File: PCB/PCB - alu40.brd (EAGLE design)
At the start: 228 x 76 mm, 163 parts, among them IC1 XB3303ASOT23, IC2 TP4054-42-SOT25-R, J1 SK-3296S-01-L1, J2 USB4510-03-1-A, Q2 PMOSFET, Q3 PMOSFET, Q5 PMOSFET, Q6 NMOSFET, U1 ISP1807-LRISP1807-LR_ISP1807-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, X1 BM02B-SRSS-TB

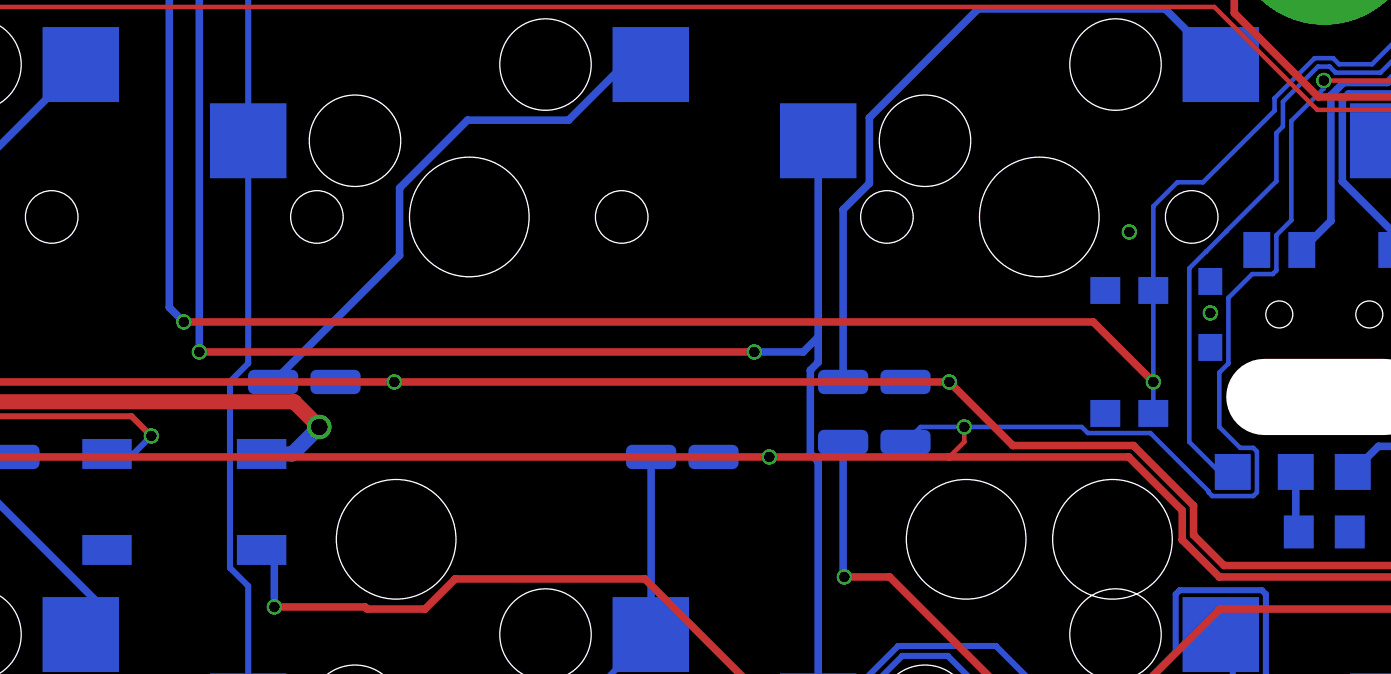
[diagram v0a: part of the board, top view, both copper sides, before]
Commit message: Move reset switch
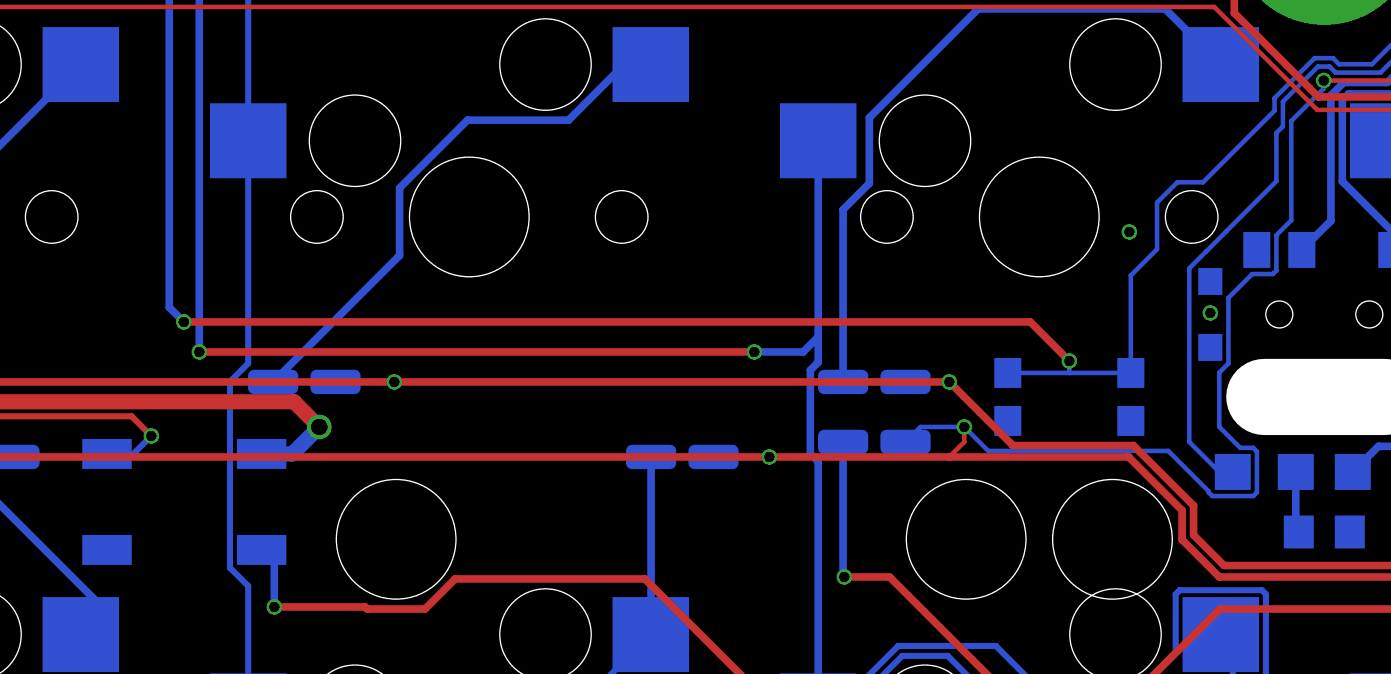
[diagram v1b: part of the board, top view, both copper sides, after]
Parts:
- moved S5 2.50 mm to (105.5, 22.5), turned to 0 degrees
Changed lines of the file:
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@@
 <attribute name="NAME" x="151.3" y="58.7" size="1.27" layer="26" rot="MR180" align="center"/>
 </element>
-<element name="S5" library="Volume_V1" library_urn="urn:adsk.eagle:library:32198814" package="TACTILE_SWITCH_SMD_4.6X2.8MM" package3d_urn="urn:adsk.eagle:package:32213842/2" value="MOMENTARY-SWITCH-SPST-SMD-4.6X2.8MM" x="107.5" y="24" smashed="yes" rot="MR90">
-<attribute name="NAME" x="109.405" y="24" size="0.6096" layer="26" font="vector" ratio="20" rot="MR90" align="bottom-center"/>
-<attribute name="PROD_ID" value="SWCH-13065" x="-31.5396" y="-53.5462" size="1.778" layer="28" rot="MR90" display="off"/>
-<attribute name="VALUE" x="105.595" y="24" size="0.6096" layer="28" font="vector" ratio="20" rot="MR90" align="top-center"/>
+<element name="S5" library="Volume_V1" library_urn="urn:adsk.eagle:library:32198814" package="TACTILE_SWITCH_SMD_4.6X2.8MM" package3d_urn="urn:adsk.eagle:package:32213842/2" value="MOMENTARY-SWITCH-SPST-SMD-4.6X2.8MM" x="105.5" y="22.5" smashed="yes" rot="MR0">
+<attribute name="NAME" x="105.5" y="24.405" size="0.6096" layer="26" font="vector" ratio="20" rot="MR0" align="bottom-center"/>
+<attribute name="PROD_ID" value="SWCH-13065" x="183.0462" y="-116.5396" size="1.778" layer="28" rot="MR0" display="off"/>
+<attribute name="VALUE" x="105.5" y="20.595" size="0.6096" layer="28" font="vector" ratio="20" rot="MR0" align="top-center"/>
 </element>
 <element name="Q5" library="Transistor" library_urn="urn:adsk.eagle:library:16378713" package="SOT23" package3d_urn="urn:adsk.eagle:package:28738/2" value="PMOSFET" x="151.5" y="41" smashed="yes" rot="MR90">
@@
 <wire x1="96.775" y1="42.35" x2="96.9471" y2="42.5221" width="0.1524" layer="16"/>
 <via x="96.9471" y="42.5221" extent="1-16" drill="0.35"/>
-<wire x1="108.3" y1="21.95" x2="108.3" y2="23" width="0.1524" layer="16"/>
-<wire x1="108.3" y1="23" x2="108.3" y2="26.05" width="0.1524" layer="16"/>
 <wire x1="81.96" y1="74.5" x2="81.96" y2="72.04" width="0.1524" layer="16"/>
 <wire x1="85.2267" y1="68.7733" x2="86.4416375" y2="68.7733" width="0.1524" layer="16"/>
@@
 <wire x1="107.4779" y1="42.5221" x2="96.9471" y2="42.5221" width="0.1524" layer="1"/>
 <wire x1="109.1012875" y1="29.6557" x2="109.9557" y2="29.6557" width="0.1524" layer="16"/>
-<wire x1="108.3" y1="26.05" x2="108.3" y2="28.8544125" width="0.1524" layer="16"/>
-<wire x1="108.3" y1="28.8544125" x2="109.1012875" y2="29.6557" width="0.1524" layer="16"/>
 <wire x1="87.65" y1="63" x2="87.65" y2="61.85" width="0.254" layer="16"/>
 <wire x1="87.65" y1="61.85" x2="88.5" y2="61" width="0.254" layer="16"/>
@@
 <wire x1="75.5" y1="25.4835" x2="75.9835" y2="25" width="0.254" layer="16"/>
 <via x="75.9835" y="25" extent="1-16" drill="0.35"/>
-<wire x1="75.9835" y1="25" x2="106.3" y2="25" width="0.254" layer="1"/>
-<wire x1="106.3" y1="25" x2="108.3" y2="23" width="0.254" layer="1"/>
-<via x="108.3" y="23" extent="1-16" drill="0.35"/>
+<wire x1="75.9835" y1="25" x2="104.2" y2="25" width="0.254" layer="1"/>
+<wire x1="104.2" y1="25" x2="105.5" y2="23.7" width="0.254" layer="1"/>
+<via x="105.5" y="23.7" extent="1-16" drill="0.35"/>
 <wire x1="112.3412" y1="32.0412" x2="112.3412" y2="32.4584125" width="0.1524" layer="16"/>
 <wire x1="112.3412" y1="32.4584125" x2="113.67485" y2="33.7920625" width="0.1524" layer="16"/>
@@
 <wire x1="114.4935875" y1="33.5906" x2="115.5906" y2="33.5906" width="0.1524" layer="16"/>
 <wire x1="109.445" y1="40.555" x2="107.4779" y2="42.5221" width="0.1524" layer="1"/>
+<wire x1="103.45" y1="23.3" x2="105.5" y2="23.3" width="0.1524" layer="16"/>
+<wire x1="105.5" y1="23.3" x2="107.55" y2="23.3" width="0.1524" layer="16"/>
+<wire x1="107.55" y1="23.3" x2="107.55" y2="26.55" width="0.1524" layer="16"/>
+<wire x1="108.4243" y1="28.9787125" x2="109.1012875" y2="29.6557" width="0.1524" layer="16"/>
+<wire x1="108.4243" y1="27.4243" x2="108.4243" y2="28.9787125" width="0.1524" layer="16"/>
+<wire x1="107.55" y1="26.55" x2="108.4243" y2="27.4243" width="0.1524" layer="16"/>
+<wire x1="105.5" y1="23.7" x2="105.5" y2="23.3" width="0.1524" layer="16"/>
 </signal>
 <signal name="POWER_PIN">
@@
 <wire x1="110.1468" y1="19.31583125" x2="110.1468" y2="19.3532" width="0.1524" layer="16"/>
 <via x="102" y="21.5" extent="1-16" drill="0.35"/>
-<wire x1="105.91263125" y1="21.5" x2="102" y2="21.5" width="0.1524" layer="16"/>
-<wire x1="106.11583125" y1="21.2968" x2="105.91263125" y2="21.5" width="0.1524" layer="16"/>
-<wire x1="108.2032" y1="21.2968" x2="106.11583125" y2="21.2968" width="0.1524" layer="16"/>
+<wire x1="108.8" y1="20.7" x2="102.8" y2="20.7" width="0.1524" layer="16"/>
+<wire x1="102" y1="21.5" x2="102.8" y2="20.7" width="0.1524" layer="16"/>
 <wire x1="102" y1="21.5" x2="102" y2="21" width="0.1524" layer="1"/>
 <wire x1="102" y1="21" x2="101.5" y2="20.5" width="0.1524" layer="1"/>
 <wire x1="110.5" y1="23.31263125" x2="110.5" y2="21.5" width="0.1524" layer="16"/>
 <wire x1="110.5" y1="21.5" x2="111.1968" y2="20.8032" width="0.1524" layer="16"/>
-<wire x1="110.1468" y1="19.3532" x2="108.2032" y2="21.2968" width="0.1524" layer="16"/>
+<wire x1="108.8" y1="20.7" x2="110.1468" y2="19.3532" width="0.1524" layer="16"/>
 <wire x1="100.04" y1="21" x2="100.54" y2="21.5" width="0.1524" layer="16"/>
 <wire x1="100.54" y1="21.5" x2="102" y2="21.5" width="0.1524" layer="16"/>

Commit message: Remove unnecessary swd pin
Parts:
- PROG1: device SparkFun-Connectors:1X06_1.27MM -> SparkFun-Connectors:1X05_1.27MM
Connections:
- net V_USB: no longer PROG1.6
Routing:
- net V_USB: track 243.9 -> 209.8 mm
- net ROW0: track 239.6 -> 240.4 mm
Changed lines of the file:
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@@
 <attribute name="VALUE" x="159.965" y="40.305" size="1.27" layer="28" rot="MR180"/>
 </element>
-<element name="PROG1" library="SparkFun-Connectors" library_urn="urn:adsk.eagle:library:513" package="1X06_1.27MM" package3d_urn="urn:adsk.eagle:package:38131/1" value="" x="84.5" y="74.5" smashed="yes" rot="MR0">
+<element name="PROG1" library="SparkFun-Connectors" library_urn="urn:adsk.eagle:library:513" package="1X05_1.27MM" package3d_urn="urn:adsk.eagle:package:38110/1" value="" x="84.5" y="74.5" smashed="yes" rot="MR0">
 <attribute name="NAME" x="84.881" y="75.516" size="0.6096" layer="26" font="vector" ratio="20" rot="MR0"/>
 <attribute name="VALUE" x="84.881" y="72.849" size="0.6096" layer="28" font="vector" ratio="20" rot="MR0"/>
@@
 <contactref element="IC2" pad="4"/>
 <contactref element="LED2" pad="A"/>
-<contactref element="PROG1" pad="6"/>
 <contactref element="D67" pad="A"/>
 <contactref element="D63" pad="2"/>
@@
 <wire x1="92.6793625" y1="45.5745" x2="93.5" y2="46.3951375" width="0.1524" layer="1"/>
 <wire x1="93.5" y1="46.3951375" x2="93.5" y2="48" width="0.1524" layer="1"/>
-<wire x1="78.15" y1="74.5" x2="79.15" y2="73.5" width="0.254" layer="1"/>
-<wire x1="102.5" y1="73.5" x2="106" y2="70" width="0.254" layer="1"/>
 <via x="126.5" y="70.5" extent="1-16" drill="0.35"/>
 <wire x1="106" y1="70" x2="119.92131875" y2="70" width="0.254" layer="1"/>
@@
 <wire x1="122.28605625" y1="72.5165" x2="124.21394375" y2="72.5165" width="0.254" layer="1"/>
 <wire x1="126.5" y1="70.5" x2="125.35" y2="70.5" width="0.254" layer="16"/>
-<wire x1="79.15" y1="73.5" x2="102.5" y2="73.5" width="0.254" layer="1"/>
 <wire x1="125.35" y1="70.5" x2="126.39" y2="71.54" width="0.508" layer="16"/>
 <wire x1="126.39" y1="71.54" x2="128.5" y2="71.54" width="0.508" layer="16"/>
@@
 <wire x1="147" y1="40.338" x2="150.112" y2="40.338" width="0.4064" layer="16"/>
 <wire x1="150.112" y1="40.338" x2="150.4" y2="40.05" width="0.4064" layer="16"/>
-<wire x1="93.5" y1="48" x2="93.5" y2="55.0165" width="0.2032" layer="16"/>
-<wire x1="93.5" y1="55.0165" x2="84" y2="64.5165" width="0.2032" layer="16"/>
-<via x="84" y="64.5165" extent="1-16" drill="0.35"/>
-<wire x1="84" y1="64.5165" x2="83.1976" y2="65.3189" width="0.2032" layer="1"/>
-<wire x1="83.1976" y1="65.3189" x2="79.93076875" y2="65.3189" width="0.2032" layer="1"/>
-<wire x1="79.93076875" y1="65.3189" x2="78.15" y2="67.09966875" width="0.2032" layer="1"/>
-<wire x1="78.15" y1="67.09966875" x2="78.15" y2="74.5" width="0.2032" layer="1"/>
+<wire x1="93.5" y1="48" x2="93.5" y2="54.9" width="0.2032" layer="16"/>
+<wire x1="93.5" y1="54.9" x2="93.5" y2="55.0165" width="0.2032" layer="16"/>
 <wire x1="150.4" y1="40.05" x2="150.95" y2="39.5" width="0.508" layer="16"/>
 <wire x1="150.95" y1="39.5" x2="152.5" y2="39.5" width="0.508" layer="16"/>
@@
 <wire x1="156.5751875" y1="60.063625" x2="157.431" y2="59.2078125" width="0.508" layer="16"/>
 <wire x1="157.7" y1="58" x2="159.15" y2="58" width="0.508" layer="16"/>
+<wire x1="93.5" y1="55.0165" x2="93.5" y2="60.6" width="0.2032" layer="16"/>
+<wire x1="93.5" y1="60.6" x2="96.9" y2="64" width="0.2032" layer="16"/>
+<via x="96.9" y="64" extent="1-16" drill="0.35"/>
+<wire x1="96.9" y1="64" x2="96.9" y2="66.5" width="0.2032" layer="1"/>
+<wire x1="100.4" y1="70" x2="106" y2="70" width="0.2032" layer="1"/>
+<wire x1="96.9" y1="66.5" x2="100.4" y2="70" width="0.2032" layer="1"/>
 </signal>
 <signal name="RESET">
@@
 <wire x1="101.54" y1="58.5" x2="99.979" y2="60.061" width="0.254" layer="16"/>
 <wire x1="99.979" y1="60.061" x2="99.979" y2="62.7752125" width="0.254" layer="16"/>
-<wire x1="99.979" y1="62.7752125" x2="98.7542125" y2="64" width="0.254" layer="16"/>
-<wire x1="98.7542125" y1="64" x2="95" y2="64" width="0.254" layer="16"/>
+<wire x1="99.979" y1="62.7752125" x2="97.7542125" y2="65" width="0.254" layer="16"/>
+<wire x1="97.7542125" y1="65" x2="96" y2="65" width="0.254" layer="16"/>
+<wire x1="96" y1="65" x2="95" y2="64" width="0.254" layer="16"/>
 <wire x1="37.04" y1="64" x2="39" y2="64" width="0.2" layer="16"/>
 <via x="39" y="64" extent="1-16" drill="0.35"/>

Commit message: Add Via
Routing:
- net GND: vias 42 -> 43
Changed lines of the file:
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@@
 <rectangle x1="56.78078125" y1="7.04021875" x2="57.2989375" y2="7.04529375" layer="25"/>
 <rectangle x1="56.8773" y1="7.045296875" x2="57.20241875" y2="7.050378125" layer="25"/>
+<wire x1="112" y1="22.5" x2="116" y2="22.5" width="2.54" layer="41"/>
+<wire x1="112" y1="22.5" x2="116" y2="22.5" width="2.54" layer="42"/>
 </plain>
 <attributes>
@@
 <attribute name="VALUE" x="108.666" y="21.9316" size="1.27" layer="28" rot="MR180" align="center"/>
 </element>
-<element name="U$1" library="Volume_V1" library_urn="urn:adsk.eagle:library:32198814" package="SINSOOM2" package3d_urn="urn:adsk.eagle:package:37877257/4" value="SINSOOM2" x="19" y="38" smashed="yes"/>
-<element name="U$2" library="Volume_V1" library_urn="urn:adsk.eagle:library:32198814" package="SINSOOM2" package3d_urn="urn:adsk.eagle:package:37877257/4" value="SINSOOM2" x="57" y="57" smashed="yes"/>
-<element name="U$3" library="Volume_V1" library_urn="urn:adsk.eagle:library:32198814" package="SINSOOM2" package3d_urn="urn:adsk.eagle:package:37877257/4" value="SINSOOM2" x="57" y="19" smashed="yes"/>
-<element name="U$4" library="Volume_V1" library_urn="urn:adsk.eagle:library:32198814" package="SINSOOM2" package3d_urn="urn:adsk.eagle:package:37877257/4" value="SINSOOM2" x="114" y="38" smashed="yes"/>
-<element name="U$5" library="Volume_V1" library_urn="urn:adsk.eagle:library:32198814" package="SINSOOM2" package3d_urn="urn:adsk.eagle:package:37877257/4" value="SINSOOM2" x="171" y="57" smashed="yes"/>
-<element name="U$6" library="Volume_V1" library_urn="urn:adsk.eagle:library:32198814" package="SINSOOM2" package3d_urn="urn:adsk.eagle:package:37877257/4" value="SINSOOM2" x="171" y="19" smashed="yes"/>
-<element name="U$7" library="Volume_V1" library_urn="urn:adsk.eagle:library:32198814" package="SINSOOM2" package3d_urn="urn:adsk.eagle:package:37877257/4" value="SINSOOM2" x="209" y="38" smashed="yes"/>
+<element name="U$1" library="Volume_V1" library_urn="urn:adsk.eagle:library:32198814" package="SINSOOM2" package3d_urn="urn:adsk.eagle:package:37877257/5" value="SINSOOM2" x="19" y="38" smashed="yes"/>
+<element name="U$2" library="Volume_V1" library_urn="urn:adsk.eagle:library:32198814" package="SINSOOM2" package3d_urn="urn:adsk.eagle:package:37877257/5" value="SINSOOM2" x="57" y="57" smashed="yes"/>
+<element name="U$3" library="Volume_V1" library_urn="urn:adsk.eagle:library:32198814" package="SINSOOM2" package3d_urn="urn:adsk.eagle:package:37877257/5" value="SINSOOM2" x="57" y="19" smashed="yes"/>
+<element name="U$4" library="Volume_V1" library_urn="urn:adsk.eagle:library:32198814" package="SINSOOM2" package3d_urn="urn:adsk.eagle:package:37877257/5" value="SINSOOM2" x="114" y="38" smashed="yes"/>
+<element name="U$5" library="Volume_V1" library_urn="urn:adsk.eagle:library:32198814" package="SINSOOM2" package3d_urn="urn:adsk.eagle:package:37877257/5" value="SINSOOM2" x="171" y="57" smashed="yes"/>
+<element name="U$6" library="Volume_V1" library_urn="urn:adsk.eagle:library:32198814" package="SINSOOM2" package3d_urn="urn:adsk.eagle:package:37877257/5" value="SINSOOM2" x="171" y="19" smashed="yes"/>
+<element name="U$7" library="Volume_V1" library_urn="urn:adsk.eagle:library:32198814" package="SINSOOM2" package3d_urn="urn:adsk.eagle:package:37877257/5" value="SINSOOM2" x="209" y="38" smashed="yes"/>
 <element name="47" library="Volume_V1" library_urn="urn:adsk.eagle:library:32198814" package="CHERRY" package3d_urn="urn:adsk.eagle:package:32198958/1" value="" x="123.5" y="9.5" smashed="yes" rot="SR0"/>
 <element name="D48" library="Volume_V1" library_urn="urn:adsk.eagle:library:32198814" package="SOD-323" package3d_urn="urn:adsk.eagle:package:32198954/3" value="1N4148WS" x="133" y="20.5" smashed="yes" rot="MR0">
@@
 <via x="80.2" y="71.5" extent="1-16" drill="0.35"/>
 <via x="144.5" y="62.7" extent="1-16" drill="0.35"/>
+<via x="116.8" y="18.3" extent="1-16" drill="0.35"/>
 </signal>
 <signal name="N$42">
